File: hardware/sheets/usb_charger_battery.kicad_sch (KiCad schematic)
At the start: 43 parts, among them J301 TYPE-C-31-M-12, J302 Battery JST-PH 2P, Q301 AO3400A, Q302 AO3400A, U301 TPD4E05U06, U302 BQ25620

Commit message: hw: state the inductor peak currents as estimates with a test gate
TI gives the TPS61023 switching frequency and valley current limit as
typical values only, so the 2.94 A boost peak depends on an assumed
0.8 MHz (the 3.8 A rating would need about 0.5 MHz) and current-limit
peaks have no datasheet bound. The charger figure now takes 100 %
efficiency as the upper bound: 3.0 A at the 1.5 A input limit, 5.7 A
at the 3.2 A power-on limit.

Measuring the switching frequency and the L202/L301 currents at full
load, start-up and overload on Rev A becomes a release gate.
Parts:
- L301: Note Same part as L202; Isat 3.8 A (10 % drop) vs 2.76 A worst-c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 -> Same part as L202; Isat 3.8 A (10 % drop) vs 3.0 A calculat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
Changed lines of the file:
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@@
 			)
 		)
-		(property "Note" "Same part as L202; Isat 3.8 A (10 % drop) vs 2.76 A worst-case peak at IINDPM 1.5 A"
+		(property "Note" "Same part as L202; Isat 3.8 A (10 % drop) vs 3.0 A calculated peak at IINDPM 1.5 A (efficiency 100 %, 1.35 MHz); measure at bring-up"
 			(at 279.4 50.8 0)
 			(hide yes)

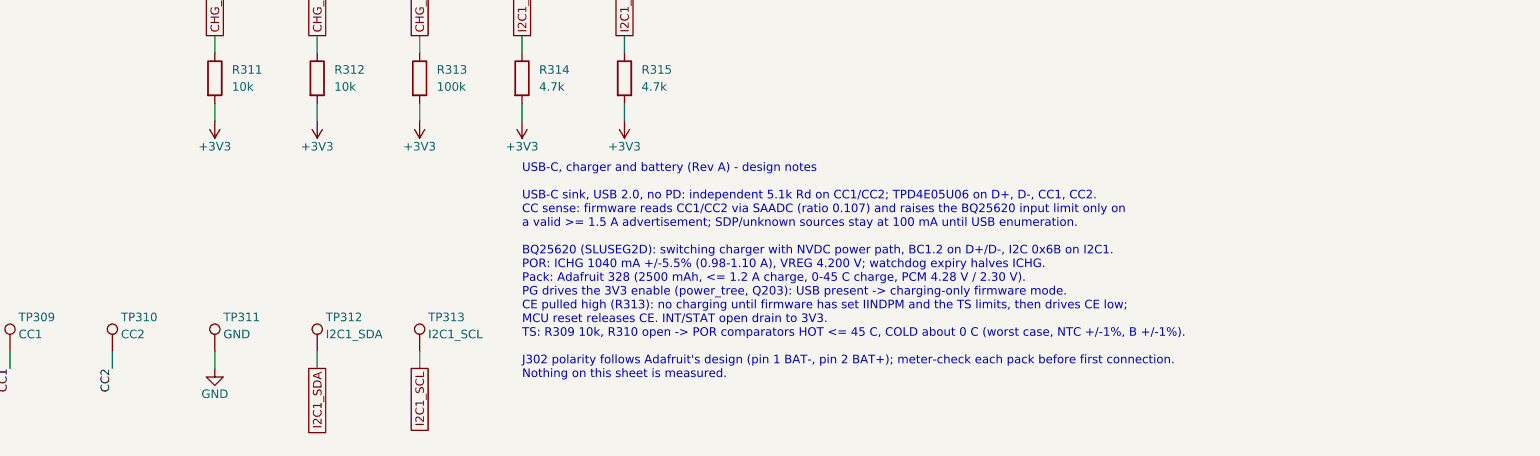
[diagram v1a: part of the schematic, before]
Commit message: hw: freeze the Rev A schematic for layout (#12)
* hw: freeze the Rev A schematic for layout

The freeze review checked every sheet against the netlist and the parts'
datasheets: rails and enables, charger and regulator capacitors, matrix
start-up and blanking, test points, USB, I2C, PDM, fault states and
back-power paths. No circuit change was needed.

The sheets' title blocks and the hardware documents now mark the
schematic as frozen for layout. Later changes go through a recorded
decision; the matrix LED footprint still follows the final LED part.
Points for bring-up include the VBUS attach capacitance, the charger
enable while 3V3 is absent, VLED loop stability and VBUS-before-VDD
behaviour.

* hw: hold the charger CE high unless the MCU enables charging

CE was pulled up to 3V3, so with USB present and the logic rail absent
(the first milliseconds after attach, or a failed 3V3 rail) it went low
and the charger charged at its reset settings, whose cold limit can be
as low as -1.5 C.

R313 now pulls CE up to SYS, which is present whenever the battery or
USB is (CE is rated to 6 V). Q303 (AO3400A) pulls CE low only while
P0.29 drives the new CHG_EN net high, and R316 holds CHG_EN low
otherwise. Charging therefore stays off in MCU reset, with the MCU
unpowered or with 3V3 missing, not only at start-up.

* fw: drive the charger enable as active-high CHG_EN

P0.29 now drives the gate of Q303 instead of the charger's CE pin, so
the board's zephyr,user property becomes chg-en-gpios, active high:
asserted means charging is allowed.

* docs: record the freeze conclusions for charging, USB and battery sensing

Charging: the CE hardware now keeps charging off without the MCU, and
the charger's reset temperature limits are never relied on.

Battery sensing: the switch, divider, leakage, ADC configuration,
settling, error budget and proposed shed margin are recorded with final
values. SAADC accuracy relies on per-board calibration.

USB: the VBUS attach capacitance (15.7 uF 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
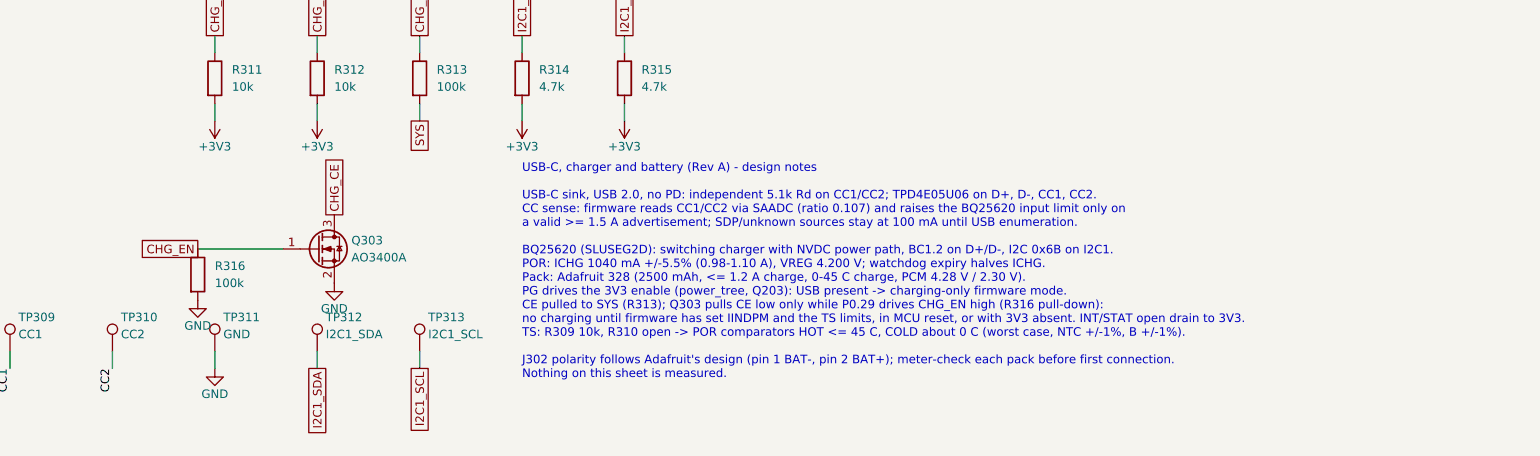
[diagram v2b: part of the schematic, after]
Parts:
- added Q303: AO3400A, Package_TO_SOT_SMD:SOT-23, symbol Transistor_FET:AO3400A
- added R316: 100k, Resistor_SMD:R_0402_1005Metric, symbol Device:R
- R313: Note CE high: charging off until firmware configures the charger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 -> CE pull-up to SYS: charging off unless Q303 is on (MCU driv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
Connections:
- net +3V3: no longer R313.2
- net CHG_CE: now also Q303.3 (D)
- net GND: now also Q303.2 (S), R316.2
- net SYS: now also R313.2
- new net CHG_EN: Q303.1 (G), R316.1

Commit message: hw: apply layout footprint and test-point changes to the schematic
The matrix LEDs use the KENTO-pattern footprint, L1101 the PCB coil,
MK1001 the 0.6 mm hole footprint and J301 the project HRO copy.

Removes test points that duplicate others: TP303 and TP304, TP208 and
TP506, and TP501-TP503, whose signals are on the SWD header. Also
removes H1304, which the carrier does not use. Rail and GND test points
move to 0.8 mm pads.

nRESET now connects only the header's open-collector pin and the module
input. ERC reports that as not driven, so the error is excluded: the
nRF5340 has an internal pull-up on reset.
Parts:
- removed TP303: SYS, TestPoint:TestPoint_Pad_D1.0mm, symbol Connector:TestPoint
- removed TP304: VBAT, TestPoint:TestPoint_Pad_D1.0mm, symbol Connector:TestPoint
- J301: footprint Connector_USB:USB_C_Receptacle_HRO_TYPE-C-31-M-12 -> smart-led-badge:USB_C_Receptacle_HRO_TYPE-C-31-M-12
- TP301, TP302, TP311: footprint TestPoint:TestPoint_Pad_D1.0mm -> smart-led-badge:TestPoint_Pad_D0.8mm
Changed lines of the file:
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@@
 	(wire
 		(pts
-			(xy 60.96 205.74) (xy 60.96 208.28)
-		)
-		(stroke
-			(width 0)
-			(type default)
-		)
-	)
-	(wire
-		(pts
 			(xy 167.64 205.74) (xy 167.64 208.28)
 		)
@@
 	(wire
 		(pts
-			(xy 76.2 205.74) (xy 76.2 208.28)
-		)
-		(stroke
-			(width 0)
-			(type default)
-		)
-	)
-	(wire
-		(pts
 			(xy 45.72 205.74) (xy 45.72 208.28)
 		)
@@
 		)
 	)
-	(global_label "VBAT"
-		(shape passive)
-		(at 76.2 208.28 270)
-		(fields_autoplaced yes)
-		(effects
-			(font
-				(size 1.27 1.27)
-			)
-			(justify right)
-		)
-		(property "Intersheetrefs" "${INTERSHEET_REFS}"
-			(at 76.2 208.28 0)
-			(hide yes)
-			(show_name no)
-			(do_not_autoplace no)
-			(effects
-				(font
-					(size 1.27 1.27)
-				)
-			)
-		)
-	)
 	(global_label "I2C1_SCL"
 		(shape passive)
@@
 		)
 	)
-	(global_label "SYS"
-		(shape passive)
-		(at 60.96 208.28 270)
-		(fields_autoplaced yes)
-		(effects
-			(font
-				(size 1.27 1.27)
-			)
-			(justify right)
-		)
-		(property "Intersheetrefs" "${INTERSHEET_REFS}"
-			(at 60.96 208.28 0)
-			(hide yes)
-			(show_name no)
-			(do_not_autoplace no)
-			(effects
-				(font
-					(size 1.27 1.27)
-				)
-			)
-		)
-	)
 	(global_label "CHG_PG_N"
 		(shape passive)
@@
 			)
 		)
-		(property "Footprint" "Connector_USB:USB_C_Receptacle_HRO_TYPE-C-31-M-12"
+		(property "Footprint" "smart-led-badge:USB_C_Receptacle_HRO_TYPE-C-31-M-12"
 			(at 33.02 76.2 0)
 			(hide yes)
@@
 			)
 		)
-		(property "Footprint" "TestPoint:TestPoint_Pad_D1.0mm"
+		(property "Footprint" "smart-led-badge:TestPoint_Pad_D0.8mm"
 			(at 182.88 205.74 0)
 			(hide yes)
@@
 	)
 	(symbol
-		(lib_id "Connector:TestPoint")
-		(at 60.96 205.74 0)
-		(unit 1)
-		(body_style 1)
-		(exclude_from_sim no)
-		(in_bom yes)
-		(on_board yes)
-		(in_pos_files yes)
-		(dnp no)
-		(property "Reference" "TP303"
-			(at 62.23 200.66 0)
-			(show_name no)
-			(do_not_autoplace no)
-			(effects
-				(font
-					(size 1.27 1.27)
-				)
-				(justify left)
-			)
-		)
-		(property "Value" "SYS"
-			(at 62.23 203.2 0)
-			(show_name no)
-			(do_not_autoplace no)
-			(effects
-				(font
-					(size 1.27 1.27)
-				)
-				(justify left)
-			)
-		)
-		(property "Footprint" "TestPoint:TestPoint_Pad_D1.0mm"
-			(at 60.96 205.74 0)
-			(hide yes)
-			(show_name no)
-			(do_not_autoplace no)
-			(effects
-				(font
-					(size 1.27 1.27)
-				)
-			)
-		)
-		(property "Datasheet" ""
-			(at 60.96 205.74 0)
-			(hide yes)
-			(show_name no)
-			(do_not_autoplace no)
-			(effects
-				(font
-					(size 1.27 1.27)
-				)
-			)
-		)
-		(property "Description" "test point"
-			(at 60.96 205.74 0)
-			(hide yes)
-			(show_name no)
-			(do_not_autoplace no)
-			(effects
-				(font
-					(size 1.27 1.27)
-				)
-			)
-		)
-		(pin "1"
-		)
-		(instances
-			(project "smart-led-badge"
-				(path "/fefc8d4a-8637-4143-b210-9149e35f9884/f79dd5bf-1129-4160-8b1f-c78c0c86307a"
-					(reference "TP303")
-					(unit 1)
-				)
-			)
-		)
-	)
-	(symbol
 		(lib_id "Device:R")
 		(at 289.56 132.08 0)
@@
 			)
 		)
-		(property "Footprint" "TestPoint:TestPoint_Pad_D1.0mm"
+		(property "Footprint" "smart-led-badge:TestPoint_Pad_D0.8mm"
 			(at 30.48 205.74 0)
 			(hide yes)
@@
 			)
 		)
-		(property "Footprint" "TestPoint:TestPoint_Pad_D1.0mm"
+		(property "Footprint" "smart-led-badge:TestPoint_Pad_D0.8mm"
 			(at 45.72 205.74 0)
 			(hide yes)
@@
 					(unit 1)
 				)
-			)
-		)
-	)
-	(symbol
-		(lib_id "Connector:TestPoint")
-		(at 76.2 205.74 0)
-		(unit 1)
-		(body_style 1)
-		(exclude_from_sim no)
-		(in_bom yes)
-		(on_board yes)
-		(in_pos_files yes)
-		(dnp no)
-		(property "Reference" "TP304"
-			(at 77.47 200.66 0)
-			(show_name no)
-			(do_not_autoplace no)
-			(effects
-				(font
-					(size 1.27 1.27)
-				)
-				(justify left)
-			)
-		)
-		(property "Value" "VBAT"
-			(at 77.47 203.2 0)
-			(show_name no)
-			(do_not_autoplace no)
-			(effects
-				(font
-					(size 1.27 1.27)
-				)
-				(justify left)
-			)
-		)
-		(property "Footprint" "TestPoint:TestPoint_Pad_D1.0mm"
-			(at 76.2 205.74 0)
-			(hide yes)
-			(show_name no)
-			(do_not_autoplace no)
-			(effects
-				(font
-					(size 1.27 1.27)
-				)
-			)
-		)
-		(property "Datasheet" ""
-			(at 76.2 205.74 0)
-			(hide yes)
-			(show_name no)
-			(do_not_autoplace no)
-			(effects
-				(font
-					(size 1.27 1.27)
-				)
-			)
-		)
-		(property "Description" "test point"
-			(at 76.2 205.74 0)
-			(hide yes)
-			(show_name no)
-			(do_not_autoplace no)
-			(effects
-				(font
-					(size 1.27 1.27)
-				)
-			)
-		)
-		(pin "1"
-		)
-		(instances
-			(project "smart-led-badge"
-				(path "/fefc8d4a-8637-4143-b210-9149e35f9884/f79dd5bf-1129-4160-8b1f-c78c0c86307a"
-					(reference "TP304")
-					(unit 1)
-				)

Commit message: hw: switch U401 to the E73 nRF52840 module
The MDBT53-P1M cannot be sourced in time for the Rev A order, while
the E73-2G4M08S1C is stocked at JLCPCB (ADR 0015).

The E73 holds its DC/DC inductors and decoupling, so L401/L402 and
C403/C404 are removed. The nRF52840 has no internal 32.768 kHz load,
so C405/C406 are fitted with 12 pF; the value is calculated and still
needs checking against the Product Specification. All 29 module GPIO
are used: CHG_STAT is no longer read by the MCU, and the UART pads,
spare GPIO pads and IMU SPI-fallback links are removed. Pins Ebyte
marks as low-frequency carry only analog inputs or slow signals.
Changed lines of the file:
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@@
 		(comment 2 "Schematic frozen for layout after review 2026-10-07; not for fabrication until the release gate")
 	)
-	(text "USB-C, charger and battery (Rev A) - design notes\n\nUSB-C sink, USB 2.0, no PD: independent 5.1k Rd on CC1/CC2; TPD4E05U06 on D+, D-, CC1, CC2.\nCC sense: firmware reads CC1/CC2 via SAADC (ratio 0.107) and raises the BQ25620 input limit only on\na valid >= 1.5 A advertisement; SDP/unknown sources stay at 100 mA until USB enumeration.\n\nBQ25620 (SLUSEG2D): switching charger with NVDC power path, BC1.2 on D+/D-, I2C 0x6B on I2C1.\nPOR: ICHG 1040 mA +/-5.5% (0.98-1.10 A), VREG 4.200 V; watchdog expiry halves ICHG.\nPack: Adafruit 328 (2500 mAh, <= 1.2 A charge, 0-45 C charge, PCM 4.28 V / 2.30 V).\nPG drives the 3V3 enable (power_tree, Q203): USB present -> charging-only firmware mode.\nCE pulled to SYS (R313); Q303 pulls CE low only while P0.29 drives CHG_EN high (R316 pull-down):\nno charging until firmware has set IINDPM and the TS limits, in MCU reset, or with 3V3 absent. INT/STAT open drain to 3V3.\nTS: R309 10k, R310 open -> POR comparators HOT <= 45 C, COLD about 0 C (worst case, NTC +/-1%, B +/-1%).\n\nJ302 polarity follows Adafruit's design (pin 1 BAT-, pin 2 BAT+); meter-check each pack before first connection.\nNothing on this sheet is measured."
+	(text "USB-C, charger and battery (Rev A) - design notes\n\nUSB-C sink, USB 2.0, no PD: independent 5.1k Rd on CC1/CC2; TPD4E05U06 on D+, D-, CC1, CC2.\nCC sense: firmware reads CC1/CC2 via SAADC (ratio 0.107) and raises the BQ25620 input limit only on\na valid >= 1.5 A advertisement; SDP/unknown sources stay at 100 mA until USB enumeration.\n\nBQ25620 (SLUSEG2D): switching charger with NVDC power path, BC1.2 on D+/D-, I2C 0x6B on I2C1.\nPOR: ICHG 1040 mA +/-5.5% (0.98-1.10 A), VREG 4.200 V; watchdog expiry halves ICHG.\nPack: Adafruit 328 (2500 mAh, <= 1.2 A charge, 0-45 C charge, PCM 4.28 V / 2.30 V).\nPG drives the 3V3 enable (power_tree, Q203): USB present -> charging-only firmware mode.\nCE pulled to SYS (R313); Q303 pulls CE low only while P0.31 drives CHG_EN high (R316 pull-down):\nno charging until firmware has set IINDPM and the TS limits, in MCU reset, or with 3V3 absent. INT/STAT open drain to 3V3.\nTS: R309 10k, R310 open -> POR comparators HOT <= 45 C, COLD about 0 C (worst case, NTC +/-1%, B +/-1%).\n\nJ302 polarity follows Adafruit's design (pin 1 BAT-, pin 2 BAT+); meter-check each pack before first connection.\nNothing on this sheet is measured."
 		(exclude_from_sim no)
 		(at 228.6 177.8 0)

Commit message: hw: lay out and route the Rev A board (#29)
* hw: add fab-layer references to custom footprints

Show each part's reference on F.Fab so the assembly drawing used for
bring-up and rework labels the custom parts the same way as the KiCad
library parts. Copper, courtyards and silkscreen are unchanged.

* hw: join the NFC coil's twin pad-2 ends as a jumper

The coil's inner and outer pad-2 ends are connected by footprint copper
(the In1 crossover), which KiCad does not count as a connection, so
NFC_LB stayed unrouted. Treat the duplicate pad numbers as a jumper.
The pad 1/2 net tie is unchanged.

* hw: remove unfitted parts and spare test points

Free routing room on the Rev A board:
- remove the eight DNP row pull-down arrays (RN709-RN716) and six DNP
  passive positions (C1103, R1005, R1104, R212, R213, R310)
- remove 19 test points outside the required set that had no room on
  the routed board

No net changes and no fitted-part changes, so the assembled board and
its BOM are the same. C1102 stays as the DNP NFC tuning position.

* hw: lay out and route the Rev A board

Place and route the 118 x 76 mm four-layer board: the 32 x 32 matrix at
45 degrees on the west, the row drivers in a column beside it, and the
power, charger, NFC, IMU, microphone and E73 module on the east. In1 is
a GND plane kept solid under the regulators, charger and module; a few
low-current signals cross it elsewhere where no other layer had room.
The board uses the JLC04161H-7628 stack-up, tented vias and
0.45/0.2 mm minimum vias.

Add release silkscreen: battery polarity at J302 on both faces,
test-point net names (front where they fit, rear behind each pad),
orientation-independent control marks, the board name and a designer
monogram on the NFC coil.

DRC and schematic parity are clean. Nothing is measured yet: charger,
USB, matrix timing, RF and NFC tuning remain bring-up checks. The README
and hardware docs now give the 118 x 76 mm outline.

* hw: move three vias out of component pads

The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
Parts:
- removed R310: DNP, Resistor_SMD:R_0402_1005Metric, symbol Device:R
- removed TP302: PMID, smart-led-badge:TestPoint_Pad_D0.8mm, symbol Connector:TestPoint
- removed TP306: CHG_PG_N, TestPoint:TestPoint_Pad_D1.0mm, symbol Connector:TestPoint
- removed TP312: I2C1_SDA, TestPoint:TestPoint_Pad_D1.0mm, symbol Connector:TestPoint
- removed TP313: I2C1_SCL, TestPoint:TestPoint_Pad_D1.0mm, symbol Connector:TestPoint
